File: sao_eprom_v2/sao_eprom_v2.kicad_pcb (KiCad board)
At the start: 4 copper layers, 65.1 x 55.1 mm, 133 parts, among them J1 Conn_01x03, J2 USB_C_Receptacle_USB2.0, J3 sao_v2_addon_tht, J4 Conn_01x02, J5 I2C, J6 I2C, Q1 RE1C002UNTCL, Q2 RE1C002ZPTL, Q3 RE1C002UNTCL, Q4 RE1C002ZPTL, Q5 RE1C002UNTCL, Q6 RE1C002ZPTL, U1 W25Q128JVS, U10 AP3012, U2 RP2040, U3 24LC00, U4 74LS573, U5 multi_eprom, U6 74LVC4245A-Q100, U7 74LS573, U8 SY8079AAC, U9 AP3012, X1 SX3M12.000M20F30TNN

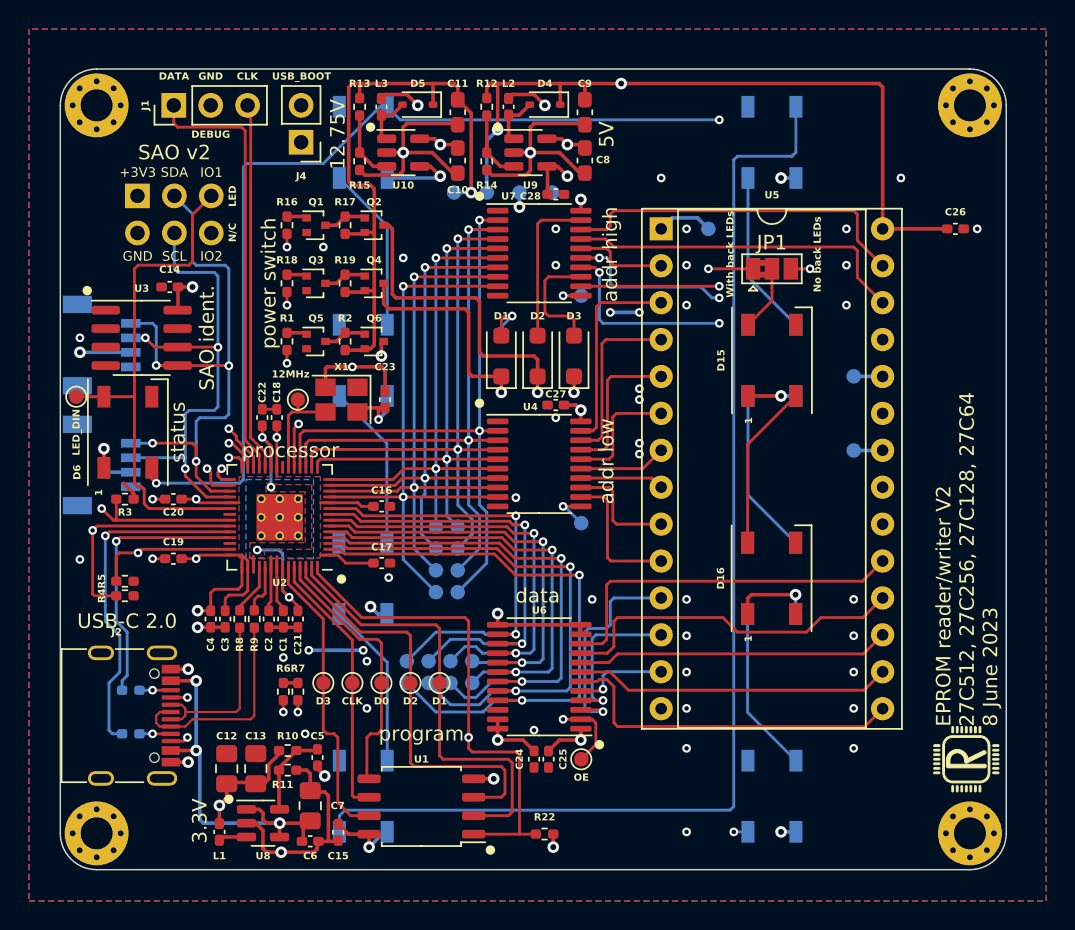
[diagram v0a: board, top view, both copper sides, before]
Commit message: Put yet another feedback in my design
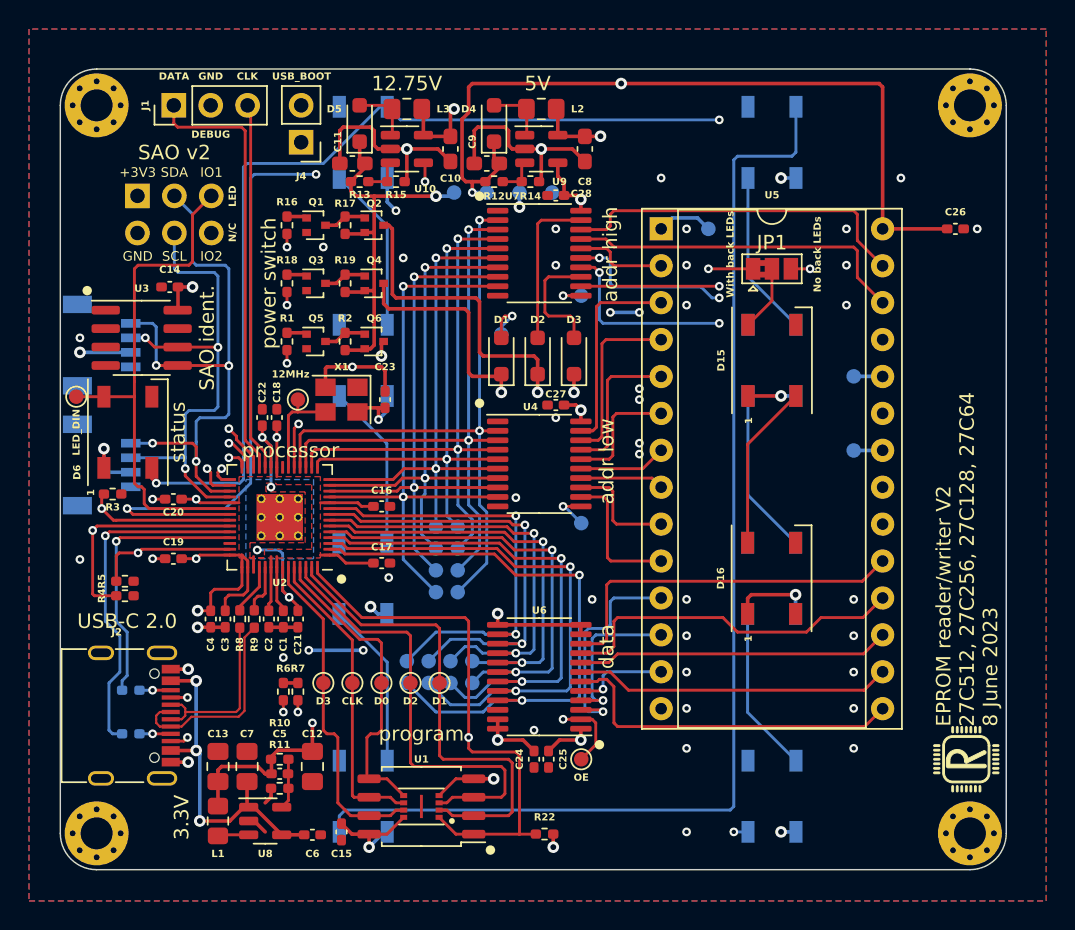
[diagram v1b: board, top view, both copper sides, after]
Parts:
- added U11: W25Q16JVUXIQ, flash:PSON50P300X200X60-9N, F.Cu at (149.5, 81.0)
- D1, D2, D3: value 1N4007 -> 1N5819WS; footprint Diode_SMD:D_SOD-123F -> Diode_SMD:D_SOD-323_HandSoldering
- D4, D5: footprint Diode_SMD:D_SOD-323 -> Diode_SMD:D_SOD-323_HandSoldering
- L1, L2, L3: footprint Inductor_SMD:L_0402_1005Metric_Pad0.77x0.64mm_HandSolder -> Inductor_SMD:L_0805_2012Metric_Pad1.15x1.40mm_HandSolder
- moved C11 8.06 mm to (144.8, 36.8), turned to 0 degrees
- moved C9 7.61 mm to (154.0, 36.8), turned to 0 degrees
- moved C12 5.90 mm to (142.0, 78.2), turned to -90 degrees
- moved R12 5.17 mm to (154.5, 38.0), turned to 180 degrees
- moved R13 5.15 mm to (145.2, 38.0), turned to 180 degrees
- moved C7 5.12 mm to (137.5, 78.2)
- moved D5 4.21 mm to (145.2, 34.0), turned to 90 degrees
- moved D4 3.73 mm to (154.5, 34.0), turned to 90 degrees
- moved R14 3.31 mm to (157.0, 38.0), turned to 180 degrees
- moved R15 2.87 mm to (147.8, 38.0), turned to 180 degrees
- moved C5 2.83 mm to (139.8, 78.8), turned to 0 degrees
- moved C13 2.60 mm to (135.5, 78.2)
- moved L2 2.25 mm to (157.8, 33.0), turned to 180 degrees
- moved L3 1.76 mm to (148.5, 33.0), turned to 180 degrees
- moved R11 1.37 mm to (139.8, 79.8), turned to 180 degrees
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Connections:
- U10 pad 4: +3V3 -> /Power generation/12V75EN
- U2 pad 35: unconnected-(U2-GPIO23-Pad35) -> /Power generation/12V75EN
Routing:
- net /Power generation/12V75EN: track 0.00 -> 51.1 mm, vias 0 -> 3
- net /Power generation/12V75: track 44.5 -> 27.8 mm
- net GND: track 76.7 -> 60.8 mm, vias 47 -> 43
- net +5V: track 104.0 -> 107.2 mm
- net /~{QSPI_CS}: track 105.5 -> 108.3 mm
- net /QSPI_D0: track 18.4 -> 21.3 mm
- net VBUS: track 26.1 -> 23.4 mm
- net /QSPI_D3: track 20.4 -> 23.0 mm
- net /QSPI_D2: track 28.9 -> 31.4 mm
- net /QSPI_D1: track 31.0 -> 33.5 mm
- net /QSPI_CLK: track 18.6 -> 21.1 mm
- net Net-(U8-FB): track 6.01 -> 3.49 mm
- net +3V3: track 129.6 -> 131.8 mm, vias 36 -> 32
- net Net-(U9-FB): track 4.81 -> 2.69 mm
- net Net-(U10-FB): track 4.81 -> 2.69 mm
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
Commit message: Phisinsh another design rephision.
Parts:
- R20, R21: moved to F.Cu
- moved R20 10.3 mm to (127.9, 65.8), turned to -90 degrees
- moved R21 7.18 mm to (128.9, 65.8), turned to -90 degrees
- moved R4 2.32 mm to (126.9, 65.8), turned to -90 degrees
- moved R5 0.97 mm to (130.0, 65.8), turned to -90 degrees
- moved C6 0.86 mm to (141.5, 82.2), turned to 90 degrees
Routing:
- net Net-(U2-GPIO26_ADC0): track 23.8 -> 11.4 mm, vias 1 -> 0
- net SBU1: track 2.15 -> 13.3 mm, vias 1 -> 0
- net Net-(U2-GPIO27_ADC1): track 18.6 -> 10.0 mm, vias 1 -> 0
- net SBU2: track 2.15 -> 9.42 mm, vias 1 -> 0
- net /Power generation/VppBEN: track 44.1 -> 41.3 mm
- net /Power generation/VdetEN: track 33.5 -> 31.9 mm
- net GND: vias 43 -> 48

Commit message: Candidate revision No. 1
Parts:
- removed TP34: TestPoint, TestPoint:TestPoint_Pad_D1.0mm
- removed X1: SX3M12.000M20F30TNN, Crystal:Crystal_SMD_3225-4Pin_3.2x2.5mm
- added C29: 22p, Capacitor_SMD:C_0402_1005Metric_Pad0.74x0.62mm_HandSolder, F.Cu at (143.5, 55.0)
- added R23: 1k, Resistor_SMD:R_0402_1005Metric_Pad0.72x0.64mm_HandSolder, F.Cu at (140.5, 52.2)
- added Y1: 12MHz, Crystal:Crystal_SMD_3225-4Pin_3.2x2.5mm, F.Cu at (144.0, 52.8)
- C23: value 100n -> 22p
- TP28: moved to B.Cu
- moved TP28 22.6 mm to (158.5, 38.8), turned to 180 degrees
- moved C23 0.35 mm to (146.8, 52.8), turned to -90 degrees
- moved C18 0.20 mm to (139.3, 54.2)
- moved C22 0.15 mm to (138.4, 54.2)
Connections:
- C23 pad 1: +3V3 -> Net-(C23-Pad1)
- TP28 pad 1: 12MHz -> GND
- U2 pad 20: 12MHz -> Net-(U2-XIN)
- U2 pad 21: unconnected-(U2-XOUT-Pad21) -> Net-(U2-XOUT)
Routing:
- net Net-(U2-XIN): track 0.00 -> 7.85 mm
- net 12MHz: track 7.07 -> 0.00 mm
- net Net-(C23-Pad1): track 0.00 -> 7.00 mm
- net GND: track 60.8 -> 55.4 mm, vias 48 -> 56
- net Net-(U2-XOUT): track 0.00 -> 5.04 mm
- net +3V3: track 131.8 -> 130.2 mm, vias 32 -> 33
- net /EPROM and level shifters/A7: track 43.9 -> 43.2 mm
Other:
- board text removed: "12MHz"

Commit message: More EPROM devving
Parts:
- added Q7: RE1C002UNTCL, Package_TO_SOT_SMD:SOT-416, F.Cu at (142.2, 40.5)
- added Q8: RE1C002ZPTL, Package_TO_SOT_SMD:SOT-416, F.Cu at (146.2, 40.5)
- added R24: 10K, Resistor_SMD:R_0402_1005Metric_Pad0.72x0.64mm_HandSolder, F.Cu at (128.4, 65.8)
- D1, D2, D3: value 1N5819WS -> 1N4007
- J1: value Conn_01x03 -> Conn_01x04; footprint Connector_PinHeader_2.54mm:PinHeader_1x03_P2.54mm_Vertical -> Connector_PinHeader_2.54mm:PinHeader_1x04_P2.54mm_Vertical
- R20: value 27R -> 1K
- R21: value 27R -> 1k
- R22: value 1K -> 100R
- R23: value 1k -> 1K
- moved J4 46.2 mm to (187.2, 39.8)
- moved R22 46.0 mm to (140.2, 40.5), turned to 90 degrees
- moved R20 34.6 mm to (158.0, 82.9), turned to 180 degrees
- moved R21 17.9 mm to (140.5, 52.2)
- moved R23 12.3 mm to (144.2, 40.5), turned to 90 degrees
- moved Q1 2.50 mm to (142.2, 43.5)
- moved Q2 2.50 mm to (146.2, 43.5)
- moved R16 2.50 mm to (140.2, 43.5)
- moved R17 2.50 mm to (144.2, 43.5)
- moved C26 2.00 mm to (186.2, 43.2)
- moved Q3 1.50 mm to (142.2, 46.5)
- moved Q4 1.50 mm to (146.2, 46.5)
- moved R18 1.50 mm to (140.2, 46.5)
- moved R19 1.50 mm to (144.2, 46.5)
- moved J1 0.83 mm to (131.6, 32.8)
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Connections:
- J1 pad 1: /SWD_DATA -> /~{QSPI_CS}
- J1 pad 2: GND -> /SWD_DATA
- J1 pad 3: /SWD_CLK -> GND
- J2 pad A8: SBU1 -> unconnected-(J2-SBU1-PadA8)
- J2 pad B8: SBU2 -> unconnected-(J2-SBU2-PadB8)
- J4 pad 2: /~{QSPI_CS} -> /Power generation/VLED
- R20 pad 1: Net-(U2-GPIO26_ADC0) -> +3V3
- R20 pad 2: SBU1 -> /~{QSPI_CS}
- R21 pad 1: Net-(U2-GPIO27_ADC1) -> Net-(C23-Pad1)
- R21 pad 2: SBU2 -> Net-(U2-XOUT)
- R22 pad 1: /~{QSPI_CS} -> /Power generation/VLEDEN
- R22 pad 2: +3V3 -> Net-(Q7-G)
- R23 pad 1: Net-(C23-Pad1) -> /Power generation/12V75
- R23 pad 2: Net-(U2-XOUT) -> Net-(Q7-D)
- U2 pad 38: Net-(U2-GPIO26_ADC0) -> /Power generation/VLEDEN
- U2 pad 39: Net-(U2-GPIO27_ADC1) -> unconnected-(U2-GPIO27_ADC1-Pad39)
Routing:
- net /Power generation/VLEDEN: track 0.00 -> 47.2 mm, vias 0 -> 2
- net /Power generation/VLED: track 0.00 -> 44.5 mm, vias 0 -> 1
- net SBU1: track 13.3 -> 0.00 mm
- net Net-(U2-GPIO26_ADC0): track 11.4 -> 0.00 mm
- net Net-(U2-GPIO27_ADC1): track 10.0 -> 0.00 mm
- net SBU2: track 9.42 -> 0.00 mm
- net +3V3: track 130.2 -> 136.2 mm, vias 33 -> 34
- net /~{QSPI_CS}: track 108.3 -> 113.8 mm
- net /SWD_DATA: track 29.9 -> 26.6 mm
- net Net-(Q7-D): track 0.00 -> 2.99 mm
- net /Power generation/12V75: track 27.8 -> 30.3 mm
- net /EPROM and level shifters/Q15: track 44.5 -> 42.0 mm
- net /Power generation/VppBEN: track 41.3 -> 39.3 mm
- net /Power generation/VppAEN: track 42.2 -> 40.4 mm
- net /EPROM and level shifters/VppB: track 46.5 -> 45.0 mm
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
